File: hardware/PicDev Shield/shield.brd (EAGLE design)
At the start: 67.5 x 50 mm, 7 parts

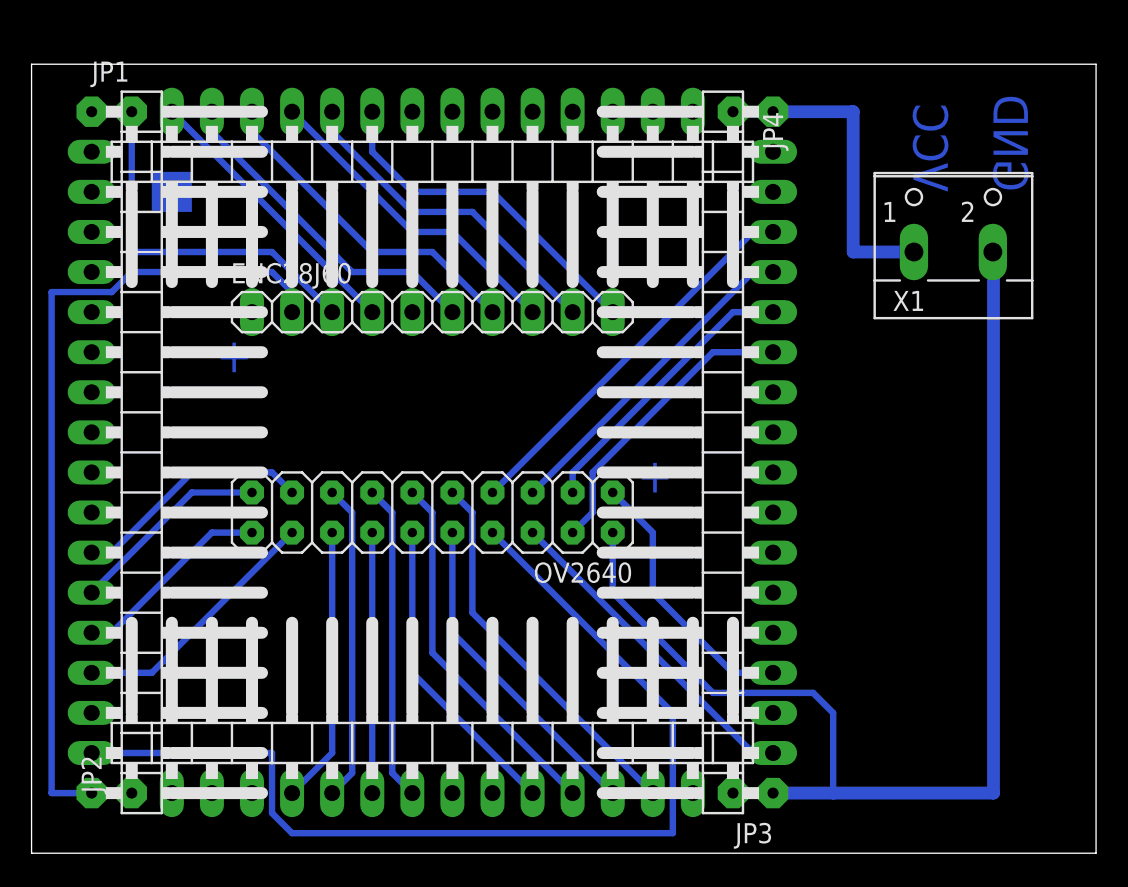
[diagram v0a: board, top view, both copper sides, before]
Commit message: Added Delay function prototype!
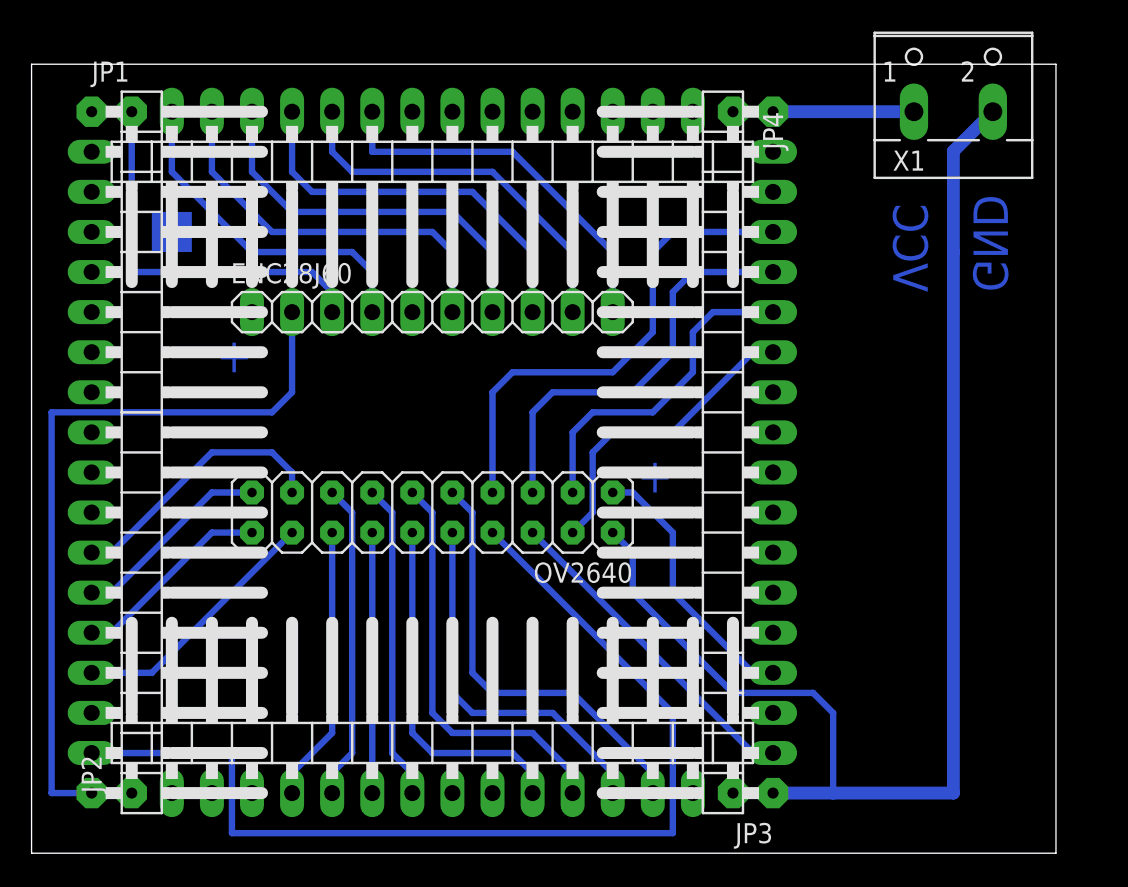
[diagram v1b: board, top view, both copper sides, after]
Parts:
- moved X1 8.89 mm to (58.4, 48.3)
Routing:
- net +5V: track 17.8 -> 8.93 mm
- net RD0: track 24.6 -> 31.3 mm
- net GND2: track 74.3 -> 80.9 mm
- net RD11: track 21.0 -> 26.2 mm
- net RE0: track 20.5 -> 25.0 mm
- net RE1: track 21.2 -> 25.0 mm
- net RE3: track 18.0 -> 21.7 mm
- net RE2: track 21.2 -> 25.0 mm
- net GND: track 51.9 -> 48.8 mm
- net RB15: track 24.3 -> 27.3 mm
- net RF1: track 21.2 -> 24.2 mm
- net RD10: track 18.2 -> 21.2 mm
- net RB14: track 20.7 -> 23.7 mm
- net RB13: track 23.3 -> 26.2 mm
- net RB12: track 19.7 -> 22.6 mm
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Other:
- board size 67.5 x 50 mm -> 64.9 x 50 mm

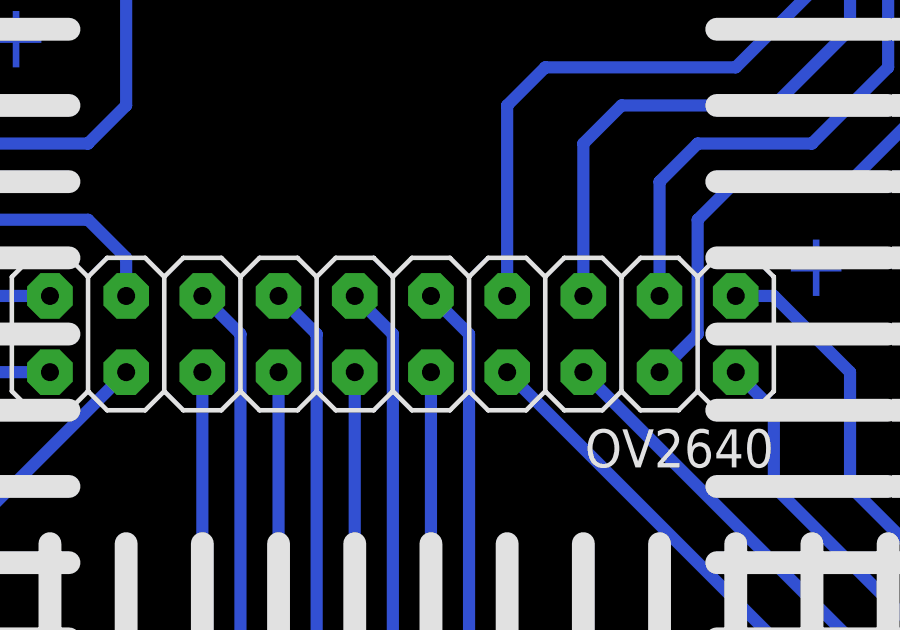
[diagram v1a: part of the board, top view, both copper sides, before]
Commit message: I2C config/new camera functions/extra debugging functions/terminal update - I2C does not work atm, but camera can be activated/deactivated.
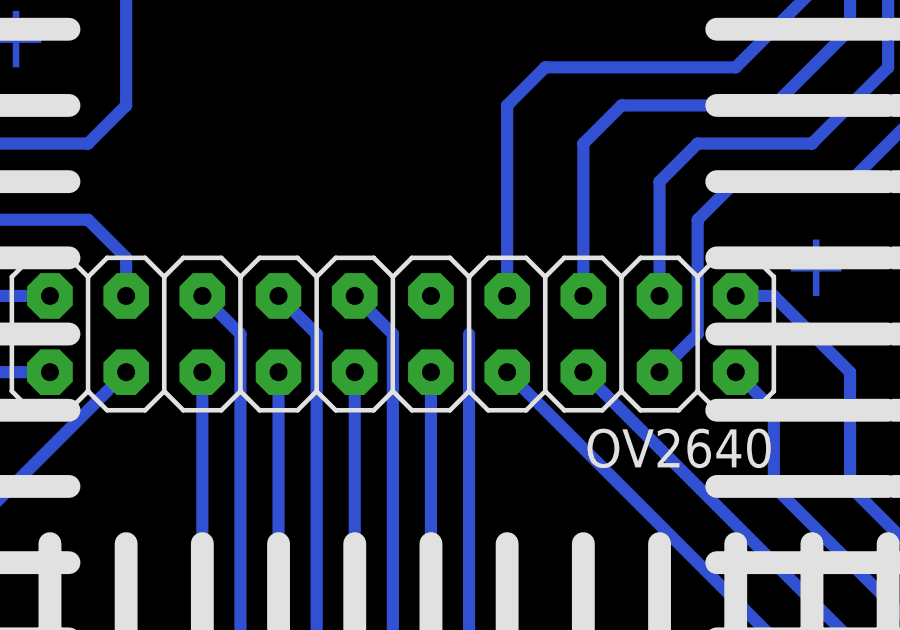
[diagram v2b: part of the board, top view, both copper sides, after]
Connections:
- removed net D+: JP3.6
- removed net D-: JP3.5
- removed net RD8: JP3.11
- removed net SOSC1: JP3.16
- removed net SOSC2: JP3.17
- net RB15: no longer OV2640.9
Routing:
- net RB15: track 27.3 -> 25.5 mm
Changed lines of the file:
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@@
 <?xml version="1.0" encoding="utf-8"?>
 <!DOCTYPE eagle SYSTEM "eagle.dtd">
-<eagle version="6.6.0">
+<eagle version="6.5.0">
 <drawing>
 <settings>
@@
 <signal name="RB15">
 <contactref element="JP2" pad="14"/>
-<contactref element="OV2640" pad="9"/>
-<wire x1="27.94" y1="21.59" x2="26.67" y2="22.86" width="0.4064" layer="16"/>
 <wire x1="27.94" y1="11.43" x2="27.94" y2="21.59" width="0.4064" layer="16"/>
 <wire x1="39.37" y1="3.81" x2="39.37" y2="5.08" width="0.4064" layer="16"/>
@@
 <wire x1="45.72" y1="6.35" x2="31.75" y2="20.32" width="0.4064" layer="16"/>
 <wire x1="46.99" y1="6.35" x2="45.72" y2="6.35" width="0.4064" layer="16"/>
-</signal>
-<signal name="RD8">
-<contactref element="JP3" pad="11"/>
 </signal>
 <signal name="RD9">
@@
 <contactref element="JP2" pad="16"/>
 </signal>
-<signal name="SOSC1">
-<contactref element="JP3" pad="16"/>
-</signal>
-<signal name="SOSC2">
-<contactref element="JP3" pad="17"/>
-</signal>
-<signal name="D+">
-<contactref element="JP3" pad="6"/>
-</signal>
-<signal name="D-">
-<contactref element="JP3" pad="5"/>
-</signal>
 <signal name="LED">
